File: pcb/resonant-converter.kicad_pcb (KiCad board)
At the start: 4 copper layers, 100 x 55 mm, 147 parts, among them J1 Banana_Jack_Keystone_575-8, J2 Banana_Jack_Keystone_575-8, J3 Banana_Jack_Keystone_575-8, J4 Banana_Jack_Keystone_575-8, J5 Molex_KK_1x4_0470531000, J6 JST_SH_1x4_BM04B-SRSS-TB-LF-SN, Q1 HSU30N20, Q2 HSU30N20, Q3 MDU04N010VRH, Q4 MDU04N010VRH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

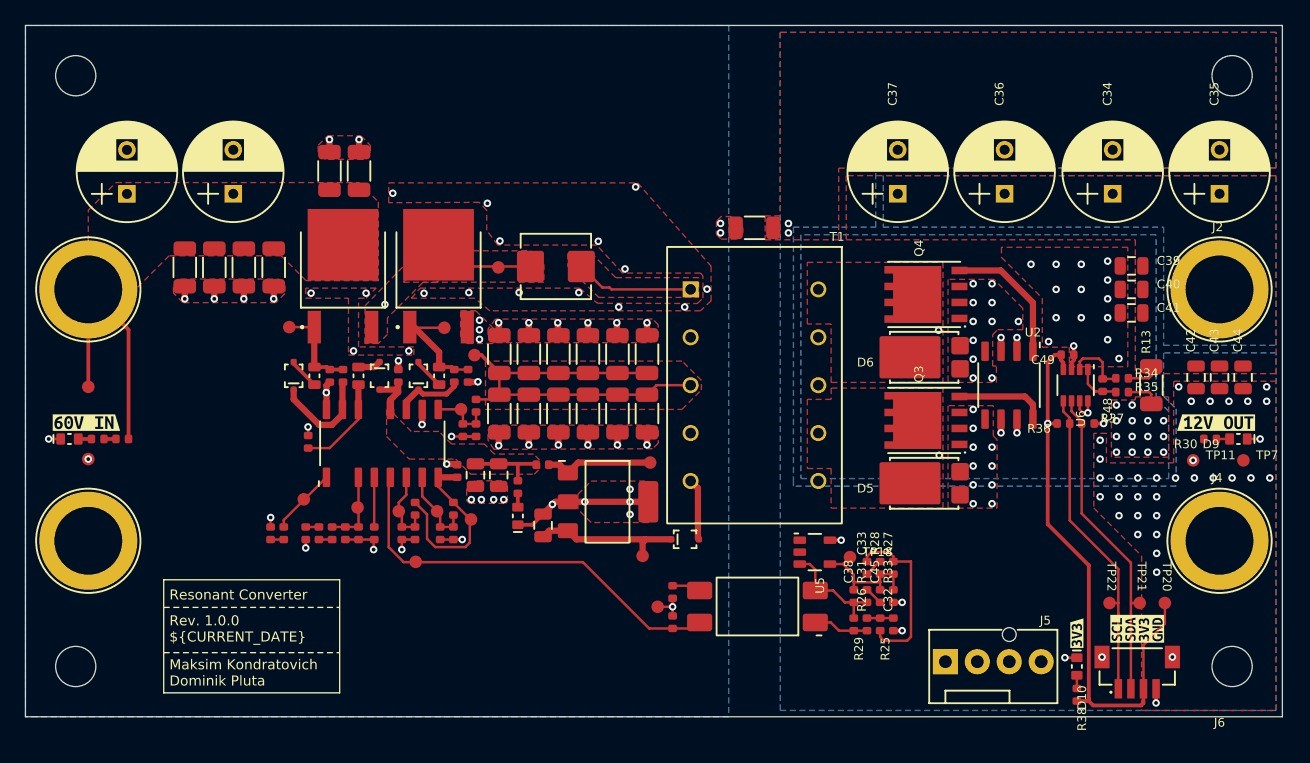
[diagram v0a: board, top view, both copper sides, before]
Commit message: PCB: Layout all secondary side connections
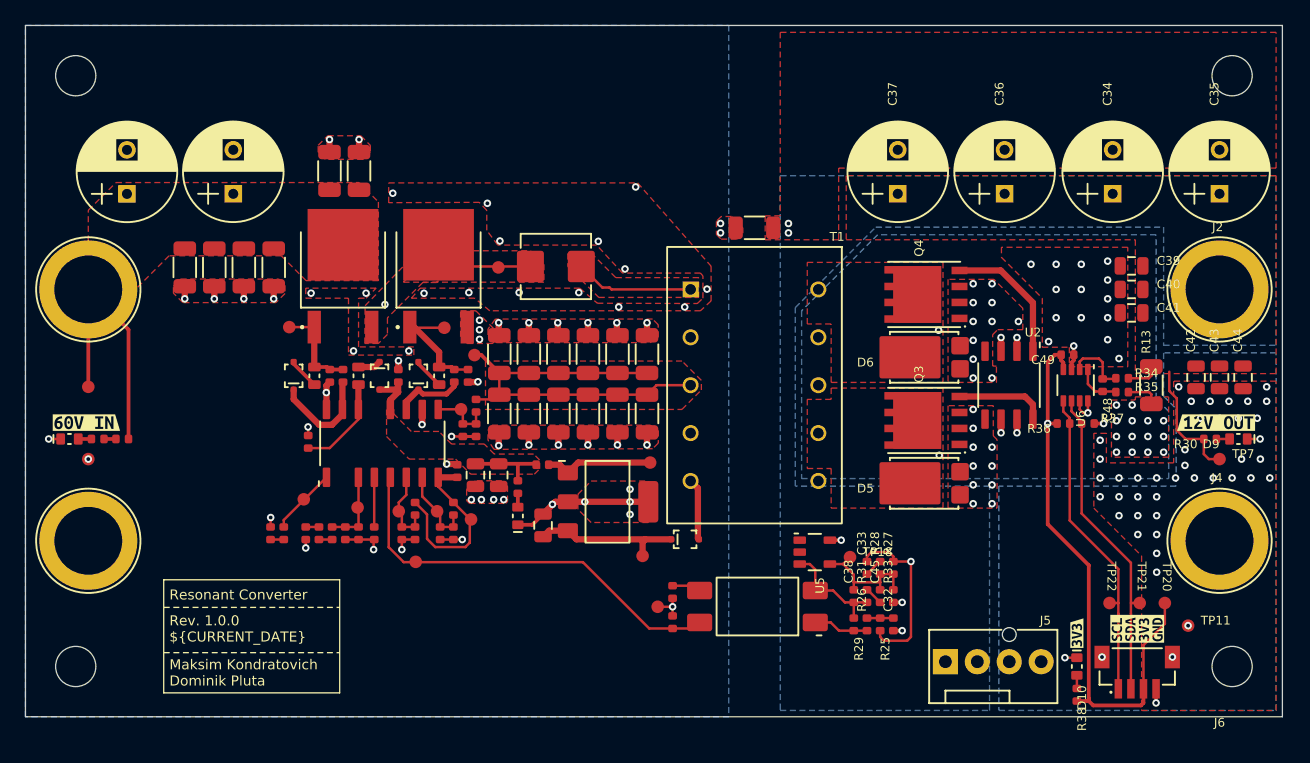
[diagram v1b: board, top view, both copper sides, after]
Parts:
- moved TP11 13.2 mm to (192.5, 116.8)
- moved TP7 1.90 mm to (195.0, 103.5)
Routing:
- net +12V: track 16.4 -> 26.4 mm, vias 0 -> 1
- net GND_ISO: vias 79 -> 87
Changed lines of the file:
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@@
 	(footprint "DW-footprints:TP_SMD_1mm"
 		(layer "F.Cu")
-		(at 196.9 103.6)
+		(at 195 103.5)
 		(descr "Test point, SMD, round,1mm diameter")
 		(tags "TEST POINT, SMD")
@@
 	(footprint "DW-footprints:TP_SMD_1mm"
 		(layer "F.Cu")
-		(at 192.9 103.6)
+		(at 192.5 116.75)
 		(descr "Test point, SMD, round,1mm diameter")
 		(tags "TEST POINT, SMD")
@@
 	)
 	(segment
+		(start 192.3 101.9)
+		(end 191.6 101.2)
+		(width 0.2)
+		(layer "F.Cu")
+		(net 14)
+	)
+	(segment
 		(start 168 117.15)
 		(end 168 117.65)
@@
 	)
 	(segment
+		(start 193.750001 101.9)
+		(end 192.3 101.9)
+		(width 0.2)
+		(layer "F.Cu")
+		(net 14)
+	)
+	(segment
+		(start 191.6 101.2)
+		(end 191.6 98.675)
+		(width 0.2)
+		(layer "F.Cu")
+		(net 14)
+	)
+	(segment
+		(start 194.15 103.5)
+		(end 193.750001 103.100001)
+		(width 0.2)
+		(layer "F.Cu")
+		(net 14)
+	)
+	(segment
 		(start 167.300001 110.900001)
 		(end 168.7 110.900001)
@@
 	)
 	(segment
+		(start 193.750001 103.100001)
+		(end 193.750001 101.9)
+		(width 0.2)
+		(layer "F.Cu")
+		(net 14)
+	)
+	(segment
 		(start 170.45 117.65)
 		(end 170.45 111.65)
@@
 	)
 	(segment
+		(start 195 103.5)
+		(end 194.15 103.5)
+		(width 0.2)
+		(layer "F.Cu")
+		(net 14)
+	)
+	(segment
 		(start 166.95 111.250001)
 		(end 167.300001 110.900001)
@@
 	)
 	(segment
+		(start 191 98.075)
+		(end 191 96.55)
+		(width 0.2)
+		(layer "F.Cu")
+		(net 14)
+	)
+	(segment
 		(start 168 117.65)
 		(end 168.3 117.95)
@@
 	)
 	(segment
+		(start 191.6 98.675)
+		(end 191 98.075)
+		(width 0.2)
+		(layer "F.Cu")
+		(net 14)
+	)
+	(segment
 		(start 168.3 117.95)
 		(end 170.15 117.95)
@@
 		(net 14)
 	)
+	(via
+		(at 170.45 111.65)
+		(size 0.6)
+		(drill 0.3)
+		(layers "F.Cu" "B.Cu")
+		(net 14)
+	)
 	(segment
 		(start 180.155 99.155)
@@
 	)
 	(via
+		(at 192.25 102.75)
+		(size 0.6)
+		(drill 0.3)
+		(layers "F.Cu" "B.Cu")
+		(net 17)
+	)
+	(via
 		(at 181.4 94.15)
 		(size 0.6)
@@
 	)
 	(via
+		(at 193.5 100.25)
+		(size 0.6)
+		(drill 0.3)
+		(layers "F.Cu" "B.Cu")
+		(net 17)
+	)
+	(via
 		(at 196 105)
 		(size 0.6)
@@
 	)
 	(via
+		(at 198 100.25)
+		(size 0.6)
+		(drill 0.3)
+		(layers "F.Cu" "B.Cu")
+		(net 17)
+	)
+	(via
 		(at 175.4 105.55)
 		(size 0.6)
@@
 	)
 	(via
+		(at 196.75 103.5)
+		(size 0.6)
+		(drill 0.3)
+		(layers "F.Cu" "B.Cu")
+		(net 17)
+	)
+	(via
 		(at 185.5 106.5)
 		(size 0.6)
@@
 	)
 	(via
+		(at 192.25 104)
+		(size 0.6)
+		(drill 0.3)
+		(layers "F.Cu" "B.Cu")
+		(net 17)
+	)
+	(via
 		(at 190 112.5)
 		(size 0.6)
@@
 	)
 	(via
+		(at 196.5 100.25)
+		(size 0.6)
+		(drill 0.3)
+		(layers "F.Cu" "B.Cu")
+		(net 17)
+	)
+	(via
 		(at 176.9 107.05)
 		(size 0.6)
@@
 	)
 	(via
-		(at 192.9 103.6)
+		(at 192.5 116.75)
 		(size 0.6)
 		(drill 0.3)
@@
 	)
 	(via
+		(at 198.25 103.5)
+		(size 0.6)
+		(drill 0.3)
+		(layers "F.Cu" "B.Cu")
+		(net 17)
+	)
+	(via
+		(at 195 100.25)
+		(size 0.6)
+		(drill 0.3)
+		(layers "F.Cu" "B.Cu")
+		(net 17)
+	)
+	(via
 		(at 164.9 109.95)
 		(size 0.6)
@@
 		(polygon
 			(pts
-				(xy 167.65 80.35) (xy 199.5 80.35) (xy 199.5 69.55) (xy 160.05 69.55) (xy 160.05 123.5) (xy 199.5 123.5)
-				(xy 199.5 95.05) (xy 190.55 95.05) (xy 190.55 98.5) (xy 191.55 99.5) (xy 191.55 105.65) (xy 161.1 105.65)
-				(xy 161.1 105.4) (xy 161.1 105.35) (xy 161.1 85.05) (xy 167.65 85.05)
+				(xy 177.45 123.5) (xy 199.5 123.5) (xy 199.5 95.05) (xy 190.55 95.05) (xy 190.55 98.5) (xy 191.55 99.5)
+				(xy 191.55 105.65) (xy 177.45 105.65)
 			)
 		)
@@
 		(polygon
 			(pts
-				(xy 199.5 80.95) (xy 168.25 80.95) (xy 168.25 85.05) (xy 190.55 85.05) (xy 190.55 94.45) (xy 199.5 94.45)
+				(xy 199.5 80.95) (xy 160.05 80.95) (xy 160.05 123.5) (xy 176.7 123.5) (xy 176.7 105.65) (xy 161.25 105.65)
+				(xy 161.25 91.45) (xy 167.65 85.05) (xy 190.55 85.05) (xy 190.55 94.45) (xy 199.5 94.45)
 			)
 		)
@@
 		(polygon
 			(pts
-				(xy 161.7 105.05) (xy 190.95 105.05) (xy 190.95 99.7) (xy 189.95 98.7) (xy 189.95 85.65) (xy 161.7 85.65)
+				(xy 161.75 91.7) (xy 161.75 105.05) (xy 190.95 105.05) (xy 190.95 99.7) (xy 189.95 98.7) (xy 189.95 85.65)
+				(xy 167.8 85.65)
 			)
 		)

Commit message: PCB: Align PCB to bigger grid, arrange component designators, add via stitching on secondary side
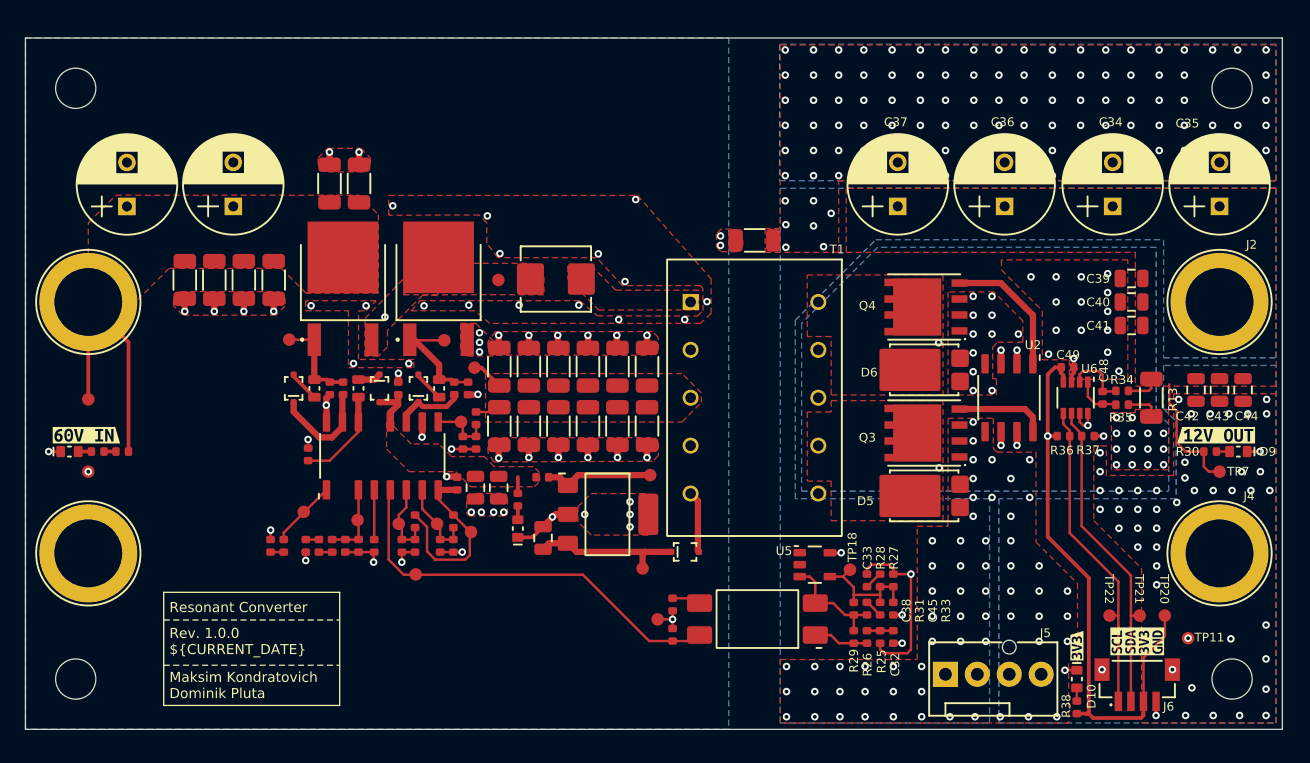
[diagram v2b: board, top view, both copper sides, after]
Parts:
- moved C1 1.00 mm to (129.7, 97.9)
- moved C10 1.00 mm to (126.5, 81.6)
- moved C11 1.00 mm to (124.2, 81.6)
- moved C12 1.00 mm to (119.8, 89.2)
- moved C13 1.00 mm to (112.7, 89.2)
- moved C14 1.00 mm to (115.0, 89.2)
- moved C15 1.00 mm to (117.4, 89.2)
- moved C16 1.00 mm to (122.5, 103.1)
- moved C17 1.00 mm to (134.3, 105.5)
- moved C18 1.00 mm to (126.5, 110.4)
- moved C19 1.00 mm to (149.4, 96.2)
- moved C2 1.00 mm to (137.7, 100.9)
- moved C20 1.00 mm to (147.1, 96.2)
- moved C21 1.00 mm to (144.8, 96.2)
- moved C22 1.00 mm to (142.4, 96.2)
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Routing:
- net /TRAFO_BOT: track 33.5 -> 4.52 mm
- net /TRAFO_TOP: track 9.45 -> 0.00 mm
- net /HS: track 23.3 -> 15.2 mm
- net GND: track 40.1 -> 33.7 mm
- net VCCP: track 10.2 -> 5.30 mm
- net GND_ISO: vias 87 -> 250

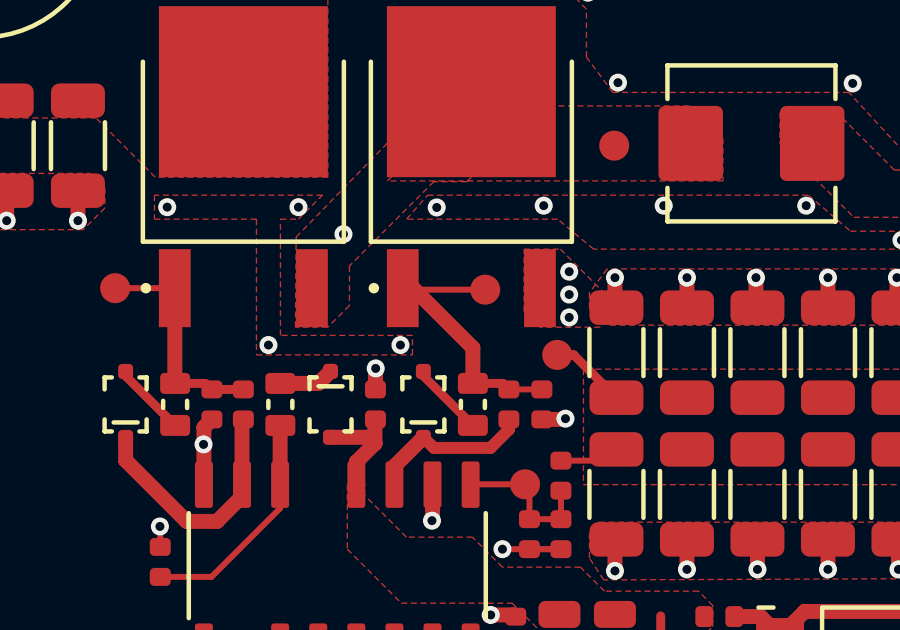
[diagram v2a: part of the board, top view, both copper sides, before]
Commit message: PCB: Clear DRC
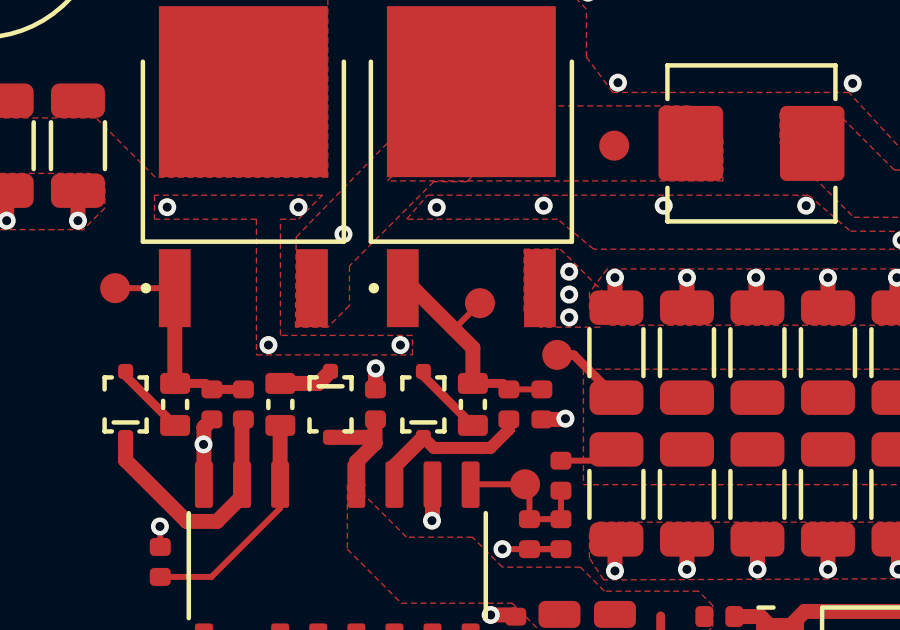
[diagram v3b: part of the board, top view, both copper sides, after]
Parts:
- moved TP6 0.48 mm to (133.2, 94.5)
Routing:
- net Net-(Q2-G): track 9.50 -> 7.95 mm
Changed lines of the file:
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@@
 	(footprint "DW-footprints:TP_SMD_1mm"
 		(layer "F.Cu")
-		(at 133.325 94.05 180)
+		(at 133.15 94.5 180)
 		(descr "Test point, SMD, round,1mm diameter")
 		(tags "TEST POINT, SMD")
@@
 		(sheetfile "resonant-converter.kicad_sch")
 		(attr through_hole)
-		(fp_poly
-			(pts
-				(xy -3.379999 -12.03) (xy 18.62 -12.03) (xy 18.62 1.87) (xy -3.38 1.87)
-			)
+		(fp_rect
+			(start -3.38 -12.03)
+			(end 18.62 1.87)
 			(stroke
 				(width 0.15)
@@
 			(layer "F.SilkS")
 		)
-		(fp_poly
-			(pts
-				(xy -3.63 -12.28) (xy 18.87 -12.28) (xy 18.87 2.119999) (xy -3.63 2.12)
-			)
+		(fp_rect
+			(start -3.63 -12.28)
+			(end 18.87 2.12)
 			(stroke
 				(width 0.05)
@@
 			(layer "F.Fab")
 		)
-		(fp_poly
-			(pts
-				(xy -3.379999 -12.03) (xy 18.62 -12.03) (xy 18.62 1.87) (xy -3.38 1.87)
-			)
+		(fp_rect
+			(start -3.38 -12.03)
+			(end 18.62 1.87)
 			(stroke
 				(width 0.15)
@@
 		)
 		(pad "4" thru_hole circle
-			(at 11.430001 0)
+			(at 11.43 0)
 			(size 1.275 1.275)
 			(drill 0.85)
@@
 		)
 		(pad "7" thru_hole circle
-			(at 11.43 -10.159999)
+			(at 11.43 -10.16)
 			(size 1.275 1.275)
 			(drill 0.85)
@@
 		(attr board_only exclude_from_pos_files allow_missing_courtyard)
 		(fp_line
-			(start -0.499999 0)
-			(end 0.499999 0)
+			(start -0.5 0)
+			(end 0.5 0)
 			(stroke
 				(width 0.1)
@@
 		)
 		(fp_line
-			(start 0 -0.499999)
-			(end 0 0.499999)
+			(start 0 -0.5)
+			(end 0 0.5)
 			(stroke
 				(width 0.1)
@@
 		(fp_circle
 			(center 0 0)
-			(end -0.499999 0)
+			(end -0.5 0)
 			(stroke
 				(width 0.1)
@@
 		(fp_circle
 			(center 3.81 0)
-			(end 3.309999 0)
+			(end 3.31 0)
 			(stroke
 				(width 0.1)
@@
 		)
 		(fp_circle
-			(center 11.430001 0)
+			(center 11.43 0)
 			(end 10.93 0)
 			(stroke
@@
 		)
 		(fp_circle
-			(center 11.43 -10.159999)
-			(end 10.93 -10.16)
+			(center 0 -10.16)
+			(end -0.5 -10.16)
 			(stroke
 				(width 0.1)
@@
 		)
 		(fp_circle
-			(center 0 -10.16)
-			(end -0.499999 -10.16)
+			(center 3.81 -10.16)
+			(end 3.31 -10.16)
 			(stroke
 				(width 0.1)
@@
 		)
 		(fp_circle
-			(center 3.81 -10.16)
-			(end 3.31 -10.159999)
+			(center 7.62 -10.16)
+			(end 7.12 -10.16)
 			(stroke
 				(width 0.1)
@@
 		)
 		(fp_circle
-			(center 7.62 -10.16)
-			(end 7.12 -10.16)
+			(center 11.43 -10.16)
+			(end 10.93 -10.16)
 			(stroke
 				(width 0.1)
@@
 		)
 		(fp_line
-			(start 0 2.300001)
+			(start 0 2.3)
 			(end 5.1 2.3)
 			(stroke
@@
 		)
 		(fp_line
-			(start 0 3.299999)
-			(end 0 2.300001)
+			(start 0 3.3)
+			(end 0 2.3)
 			(stroke
 				(width 0.15)
@@
 			(layer "F.SilkS")
 		)
-		(fp_poly
-			(pts
-				(xy -1.490001 -2.74) (xy 9.11 -2.74) (xy 9.11 3.5) (xy -1.49 3.5)
-			)
+		(fp_rect
+			(start -1.49 -2.74)
+			(end 9.11 3.5)
 			(stroke
 				(width 0.05)
@@
 		)
 		(fp_line
-			(start 0 2.300001)
-			(end 0 3.299999)
+			(start 0 2.3)
+			(end 0 3.3)
 			(stroke
 				(width 0.15)
@@
 		(fp_line
 			(start 5.1 2.3)
-			(end 0 2.300001)
+			(end 0 2.3)
 			(stroke
 				(width 0.15)
@@
 			(layer "F.Fab")
 		)
-		(fp_poly
-			(pts
-				(xy -1.29 -2.54) (xy 8.91 -2.54) (xy 8.91 3.3) (xy -1.29 3.3)
-			)
+		(fp_rect
+			(start -1.29 -2.54)
+			(end 8.91 3.3)
 			(stroke
 				(width 0.15)
@@
 		)
 		(pad "3" thru_hole circle
-			(at 5.079999 0)
+			(at 5.08 0)
 			(size 2 2)
 			(drill 1.02)
@@
 		(attr board_only exclude_from_pos_files allow_missing_courtyard)
 		(fp_line
-			(start -0.499999 0)
-			(end 0.499999 0)
+			(start -0.5 0)
+			(end 0.5 0)
 			(stroke
 				(width 0.1)
@@
 		)
 		(fp_line
-			(start 0 -0.499999)
-			(end 0 0.499999)
+			(start 0 -0.5)
+			(end 0 0.5)
 			(stroke
 				(width 0.1)
@@
 		(fp_circle
 			(center 0 0)
-			(end -0.499999 0)
+			(end -0.5 0)
 			(stroke
 				(width 0.1)
@@
 		(fp_circle
 			(center 3.81 0)
-			(end 3.309999 0)
+			(end 3.31 0)
 			(stroke
 				(width 0.1)
@@
 		)
 		(fp_circle
-			(center 11.430001 0)
+			(center 11.43 0)
 			(end 10.93 0)
 			(stroke
@@
 		)
 		(fp_circle
-			(center 11.43 -10.159999)
-			(end 10.93 -10.16)
+			(center 0 -10.16)
+			(end -0.5 -10.16)
 			(stroke
 				(width 0.1)
@@
 		)
 		(fp_circle
-			(center 0 -10.16)
-			(end -0.499999 -10.16)
+			(center 3.81 -10.16)
+			(end 3.31 -10.16)
 			(stroke
 				(width 0.1)
@@
 		)
 		(fp_circle
-			(center 3.81 -10.16)
-			(end 3.31 -10.159999)
+			(center 7.62 -10.16)
+			(end 7.12 -10.16)
 			(stroke
 				(width 0.1)
@@
 		)
 		(fp_circle
-			(center 7.62 -10.16)
-			(end 7.12 -10.16)
+			(center 11.43 -10.16)
+			(end 10.93 -10.16)
 			(stroke
 				(width 0.1)
@@
 	)
 	(segment
-		(start 133.325 94.05)
-		(end 130.628 94.05)
-		(width 0.2)
+		(start 132.2875 95.3625)
+		(end 130.925 94)
+		(width 0.5)
 		(layer "F.Cu")
 		(net 3)
@@
 	)
 	(segment
+		(start 133.15 94.5)
+		(end 132.2875 95.3625)
+		(width 0.2)
+		(layer "F.Cu")
+		(net 3)
+	)
+	(segment
 		(start 133.913998 97.175)
 		(end 132.913999 97.175)
@@
 	(segment
 		(start 132.913999 95.988999)
-		(end 130.925 94)
+		(end 132.2875 95.3625)
 		(width 0.5)
 		(layer "F.Cu")
@@
 		(layer "F.Cu")
 		(net 3)
-	)
-	(segment
-		(start 130.628 94.05)
-		(end 130.578 94)
-		(width 0.2)
-		(layer "F.Cu")
-		(net 3)
